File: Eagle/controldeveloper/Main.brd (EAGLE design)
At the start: 60 x 65 mm, 21 parts

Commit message: Final version of Eagle board
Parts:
- moved R3 3.00 mm to (31.6, 34.1)
- moved U3 0.16 mm to (41.1, 4.06), flipped to the bottom
- renumbered RX/TX to GD|RX|TX
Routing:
- net GND: track 254.5 -> 208.2 mm
- net VCC: track 193.7 -> 185.1 mm, vias 2 -> 3
- net N$7: track 26.0 -> 23.8 mm
- net EN2: track 31.8 -> 29.8 mm
- net PH2: track 57.1 -> 55.1 mm, vias 2 -> 0
- net VDD: track 100.7 -> 102.1 mm, vias 1 -> 0
- net EN1: track 29.0 -> 29.7 mm
- net PH1: vias 2 -> 0
- added copper zone on layer 16, net GND
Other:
- board text removed: "TXD RXD GND"

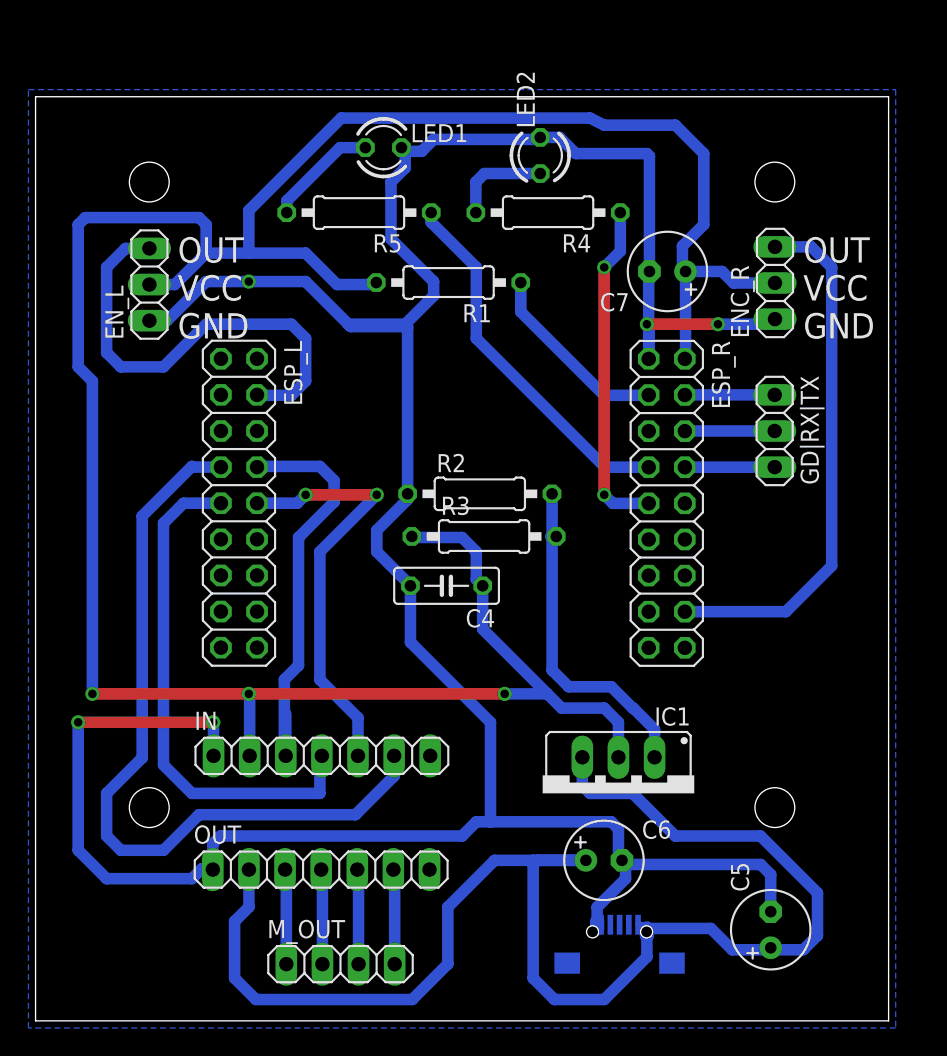
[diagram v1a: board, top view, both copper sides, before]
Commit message: Bugs in Eagle Design were corrected!
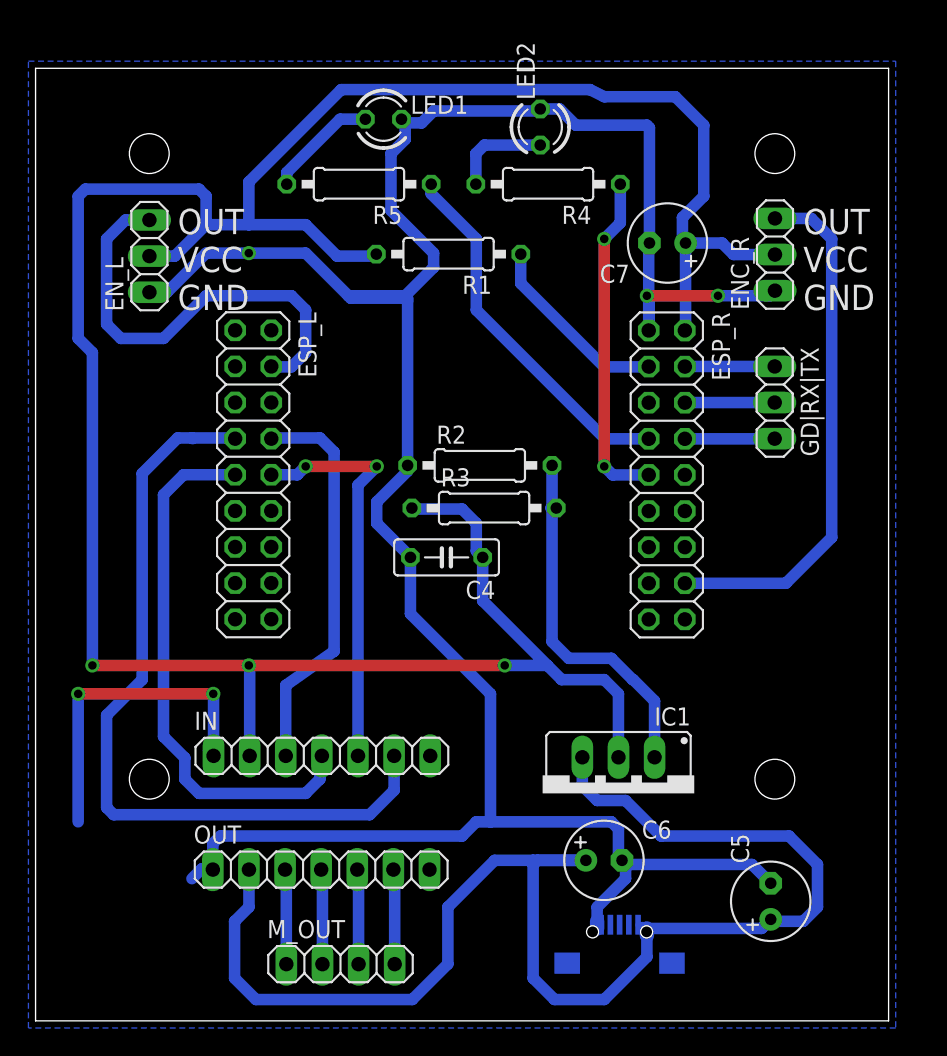
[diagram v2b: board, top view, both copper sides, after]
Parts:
- moved ESP_L 2.24 mm to (15.3, 38.4)
- moved C4 2.00 mm to (28.9, 32.6)
- moved C5 2.00 mm to (51.7, 8.41)
- moved C7 2.00 mm to (44.5, 54.7)
- moved ENC_R 2.00 mm to (52.0, 53.9)
- moved EN_L 2.00 mm to (8.01, 53.8)
- moved ESP_R 2.00 mm to (44.4, 38.4)
- moved GD|RX|TX 2.00 mm to (52.0, 43.5)
- moved LED1 2.00 mm to (24.5, 63.4)
- moved LED2 2.00 mm to (35.5, 62.9)
- moved R1 2.00 mm to (29.1, 53.9)
- moved R2 2.00 mm to (31.2, 39.1)
- moved R3 2.00 mm to (31.6, 36.1)
- moved R4 2.00 mm to (36.0, 58.9)
- moved R5 2.00 mm to (22.8, 58.9)
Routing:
- net GND: track 208.2 -> 201.0 mm
- net VCC: track 185.1 -> 189.1 mm
- net PH1: track 36.2 -> 38.3 mm
- net N$7: track 23.8 -> 25.8 mm
- net EN1: track 29.7 -> 28.1 mm
- net EN2: track 29.8 -> 28.6 mm
- net VDD: track 102.1 -> 101.1 mm
- net ENC_L: track 32.5 -> 31.5 mm
- net PH2: track 55.1 -> 56.1 mm
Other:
- board size 60 x 65 mm -> 60 x 67 mm

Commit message: **** **First RELEASE** ****
Fully working version of code and Eagle design!
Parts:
- R4, R5: value 10k -> 0.6k
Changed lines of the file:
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@@
 <layer number="24" name="bOrigins" color="15" fill="1" visible="yes" active="yes"/>
 <layer number="25" name="tNames" color="7" fill="1" visible="yes" active="yes"/>
-<layer number="26" name="bNames" color="7" fill="1" visible="no" active="yes"/>
+<layer number="26" name="bNames" color="7" fill="1" visible="yes" active="yes"/>
 <layer number="27" name="tValues" color="7" fill="1" visible="no" active="yes"/>
 <layer number="28" name="bValues" color="7" fill="1" visible="no" active="yes"/>
@@
 <element name="R2" library="rcl" package="0207/10" value="390" x="31.25" y="39.07"/>
 <element name="R3" library="rcl" package="0207/10" value="240" x="31.55" y="36.07"/>
-<element name="R4" library="rcl" package="0207/10" value="10k" x="36.05" y="58.85" rot="R180"/>
-<element name="R5" library="rcl" package="0207/10" value="10k" x="22.75" y="58.85" rot="R180"/>
+<element name="R4" library="rcl" package="0207/10" value="0.6k" x="36.05" y="58.85" rot="R180"/>
+<element name="R5" library="rcl" package="0207/10" value="0.6k" x="22.75" y="58.85" rot="R180"/>
 <element name="GD|RX|TX" library="pinhead" package="1X03" value="" x="51.99" y="43.49" rot="R270"/>
 <element name="U3" library="MicroUSB" package="USB-MICRO-SMD" value="" x="41.08" y="4.06" rot="MR90"/>

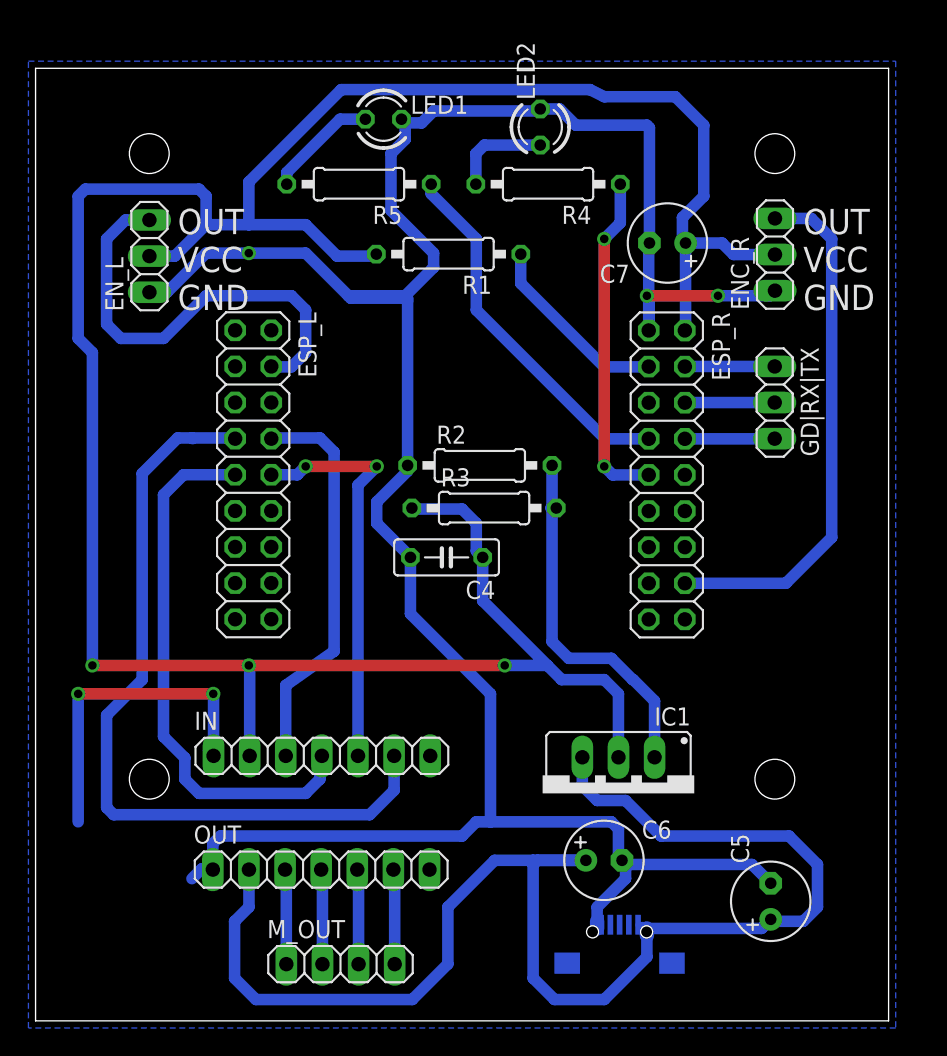
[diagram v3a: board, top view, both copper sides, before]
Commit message: ****Release*** NO MORE Radio bugs
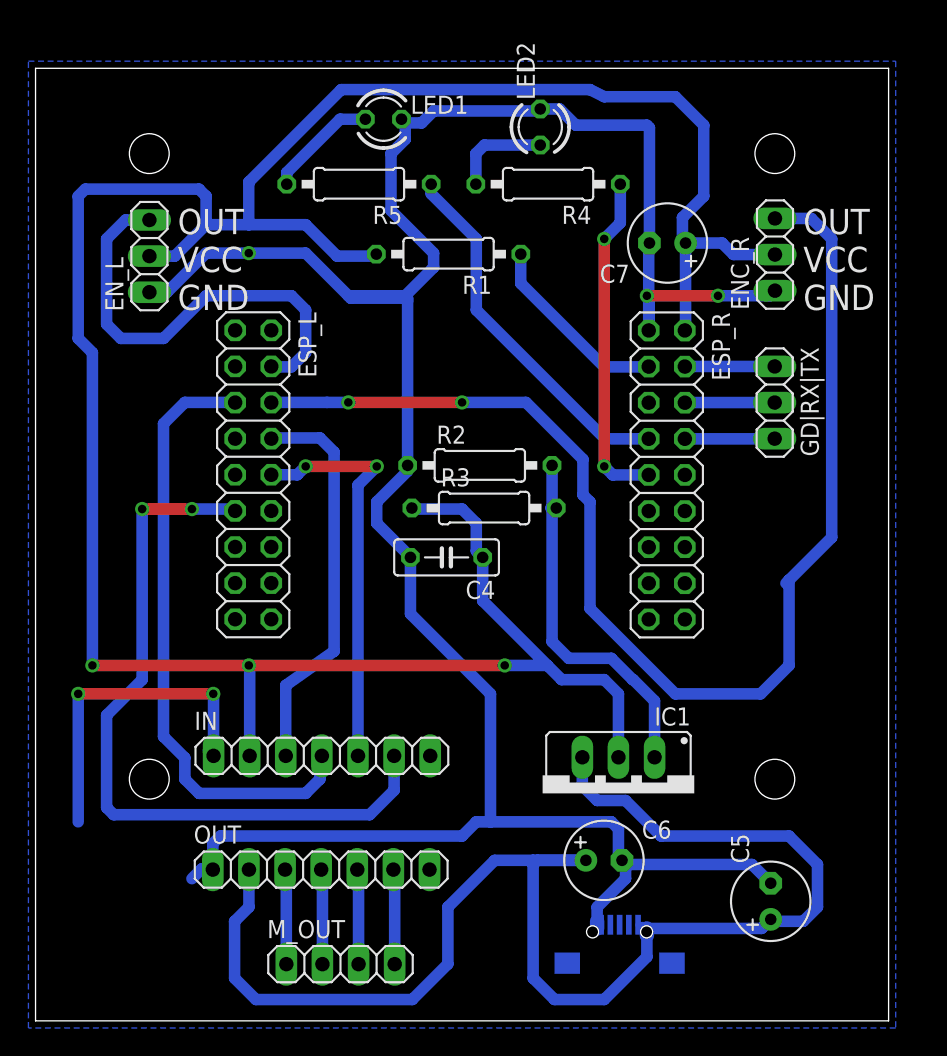
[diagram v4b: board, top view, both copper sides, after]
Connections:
- net ENC_R: now also ESP_L.6; no longer ESP_R.16
- net PH1: now also ESP_L.5; no longer ESP_L.9
- net PH2: now also ESP_L.11; no longer ESP_L.7
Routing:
- net ENC_R: track 37.3 -> 87.8 mm, vias 0 -> 2
- net PH1: track 38.3 -> 43.3 mm
- net PH2: track 56.1 -> 52.5 mm, vias 0 -> 2
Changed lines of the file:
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@@
 <signal name="ENC_R">
 <contactref element="ENC_R" pad="3"/>
-<contactref element="ESP_R" pad="16"/>
 <wire x1="52.01" y1="56.44" x2="54.56" y2="56.44" width="0.8128" layer="16"/>
 <wire x1="54.56" y1="56.44" x2="56" y2="55" width="0.8128" layer="16"/>
 <wire x1="56" y1="55" x2="56" y2="34" width="0.8128" layer="16"/>
-<wire x1="56" y1="34" x2="52.78" y2="30.78" width="0.8128" layer="16"/>
-<wire x1="45.67" y1="30.78" x2="52.78" y2="30.78" width="0.8128" layer="16"/>
+<wire x1="56" y1="34" x2="53" y2="31" width="0.8128" layer="16"/>
+<contactref element="ESP_L" pad="6"/>
+<wire x1="53" y1="31" x2="52.78" y2="30.78" width="0.8128" layer="16"/>
+<wire x1="53" y1="31" x2="53" y2="25" width="0.8128" layer="16"/>
+<wire x1="53" y1="25" x2="51" y2="23" width="0.8128" layer="16"/>
+<wire x1="51" y1="23" x2="45" y2="23" width="0.8128" layer="16"/>
+<wire x1="45" y1="23" x2="39" y2="29" width="0.8128" layer="16"/>
+<wire x1="39" y1="29" x2="39" y2="36.5" width="0.8128" layer="16"/>
+<wire x1="39" y1="36.5" x2="38.5" y2="37" width="0.8128" layer="16"/>
+<wire x1="38.5" y1="37" x2="38.5" y2="39.5" width="0.8128" layer="16"/>
+<wire x1="38.5" y1="39.5" x2="34.5" y2="43.5" width="0.8128" layer="16"/>
+<wire x1="34.5" y1="43.5" x2="30" y2="43.5" width="0.8128" layer="16"/>
+<wire x1="30" y1="43.5" x2="22" y2="43.5" width="0.8128" layer="1"/>
+<wire x1="22" y1="43.5" x2="20.5" y2="43.5" width="0.8128" layer="16"/>
+<wire x1="16.5" y1="43.5" x2="20.5" y2="43.5" width="0.8128" layer="16"/>
+<via x="22" y="43.5" extent="1-16" drill="0.6" shape="square"/>
+<via x="30" y="43.5" extent="1-16" drill="0.6" shape="square"/>
+<wire x1="16.5" y1="43.5" x2="16.58" y2="43.49" width="0" layer="19" extent="16-16"/>
 </signal>
 <signal name="ENC_L">
@@
 <signal name="PH1">
 <contactref element="IN" pad="4"/>
-<contactref element="ESP_L" pad="9"/>
-<wire x1="9" y1="37" x2="9" y2="20" width="0.8128" layer="16"/>
+<wire x1="9" y1="42" x2="9" y2="20" width="0.8128" layer="16"/>
 <wire x1="20" y1="18.5" x2="20.14" y2="18.64" width="0.8128" layer="16"/>
-<wire x1="14.04" y1="38.41" x2="10.41" y2="38.41" width="0.8128" layer="16"/>
-<wire x1="10.41" y1="38.41" x2="9" y2="37" width="0.8128" layer="16"/>
 <wire x1="20" y1="18.5" x2="20" y2="17" width="0.8128" layer="16"/>
 <wire x1="20" y1="17" x2="19" y2="16" width="0.8128" layer="16"/>
@@
 <wire x1="10.5" y1="17" x2="10.5" y2="18.5" width="0.8128" layer="16"/>
 <wire x1="10.5" y1="18.5" x2="9" y2="20" width="0.8128" layer="16"/>
+<contactref element="ESP_L" pad="5"/>
+<wire x1="9" y1="42" x2="10.5" y2="43.5" width="0.8128" layer="16"/>
+<wire x1="10.5" y1="43.5" x2="14.03" y2="43.5" width="0.8128" layer="16"/>
+<wire x1="14.03" y1="43.5" x2="14.04" y2="43.49" width="0.8128" layer="16"/>
 </signal>
 <signal name="EN2">
@@
 <signal name="PH2">
 <contactref element="IN" pad="6"/>
-<contactref element="ESP_L" pad="7"/>
 <wire x1="25" y1="18.42" x2="25.22" y2="18.64" width="0.8128" layer="16"/>
 <wire x1="25.22" y1="18.64" x2="25.22" y2="16.22" width="0.8128" layer="16"/>
-<wire x1="7.5" y1="24" x2="7.5" y2="38.5" width="0.8128" layer="16"/>
-<wire x1="11.05" y1="40.95" x2="11" y2="41" width="0.8128" layer="16"/>
-<wire x1="7.5" y1="38.5" x2="10" y2="41" width="0.8128" layer="16"/>
-<wire x1="10" y1="41" x2="11" y2="41" width="0.8128" layer="16"/>
-<wire x1="11" y1="41" x2="13.99" y2="41" width="0.8128" layer="16"/>
-<wire x1="13.99" y1="41" x2="14.04" y2="40.95" width="0.8128" layer="16"/>
 <wire x1="25.22" y1="16.22" x2="23.5" y2="14.5" width="0.8128" layer="16"/>
 <wire x1="23.5" y1="14.5" x2="5.5" y2="14.5" width="0.8128" layer="16"/>
@@
 <wire x1="5" y1="15" x2="5" y2="21.5" width="0.8128" layer="16"/>
 <wire x1="5" y1="21.5" x2="7.5" y2="24" width="0.8128" layer="16"/>
+<contactref element="ESP_L" pad="11"/>
+<wire x1="7.5" y1="24" x2="7.5" y2="36" width="0.8128" layer="16"/>
+<via x="7.5" y="36" extent="1-16" drill="0.6" shape="square"/>
+<wire x1="7.5" y1="36" x2="11" y2="36" width="0.8128" layer="1"/>
+<via x="11" y="36" extent="1-16" drill="0.6" shape="square"/>
+<wire x1="11" y1="36" x2="13.91" y2="36" width="0.8128" layer="16"/>
+<wire x1="13.91" y1="36" x2="14.04" y2="35.87" width="0.8128" layer="16"/>
 </signal>
 <signal name="N$12">

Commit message: Eagle PCB Redesigned
* Routes were optimized
* Space for heat sink added
* Added Power ON/OFF switch
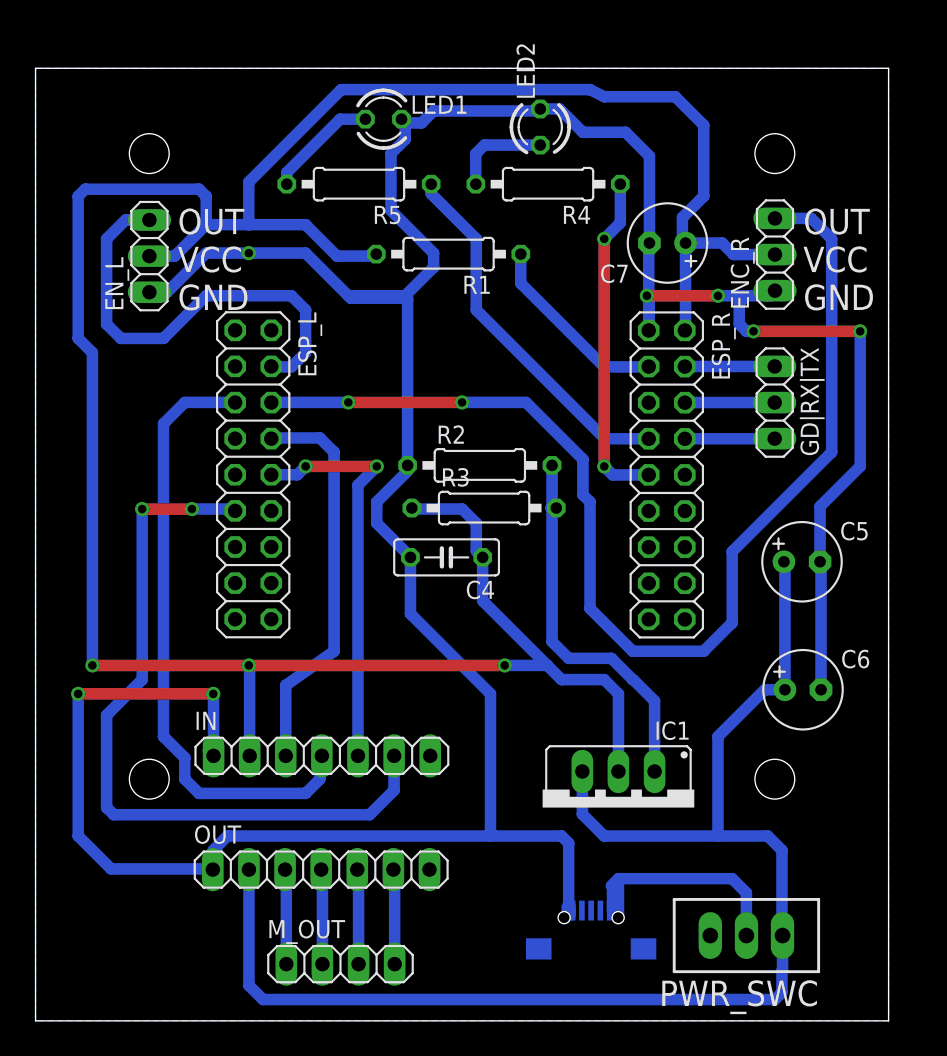
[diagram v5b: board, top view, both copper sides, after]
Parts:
- added PWR_SWC: TL32PO, switch:TL3XPO
- moved C5 24.0 mm to (53.9, 32.3), turned to 0 degrees
- moved C6 18.4 mm to (54.0, 23.3)
- moved U3 2.24 mm to (39.1, 5.06)
- moved IC1 1.00 mm to (41.0, 15.0)
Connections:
- new net N$11: PWR_SWC.2, U3.VBUS1
- net VDD: now also PWR_SWC.1; no longer U3.VBUS1
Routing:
- net GND: track 201.0 -> 230.0 mm, vias 5 -> 7
- net N$11: track 0.00 -> 18.4 mm
- net ENC_R: track 87.8 -> 80.9 mm
- net VDD: track 101.1 -> 96.5 mm
- net N$9: track 0.00 -> 2.00 mm
- net VCC: track 189.1 -> 190.1 mm
- net N$7: track 25.8 -> 26.8 mm
- added copper zone on layer 16, net N$14
- removed copper zone on layer 16, net GND
